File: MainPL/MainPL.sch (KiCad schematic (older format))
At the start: 37 parts, among them J1 Conn_01x06_Female, J10 Conn_01x06_Female, J11 Conn_01x06_Female, J12 Conn_01x06_Female, J13 Conn_01x06_Female, J14 Conn_01x06_Female, J15 Conn_01x01_Male, J16 Conn_01x04_Male, J2 USB_B, J3 Conn_01x06_Female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

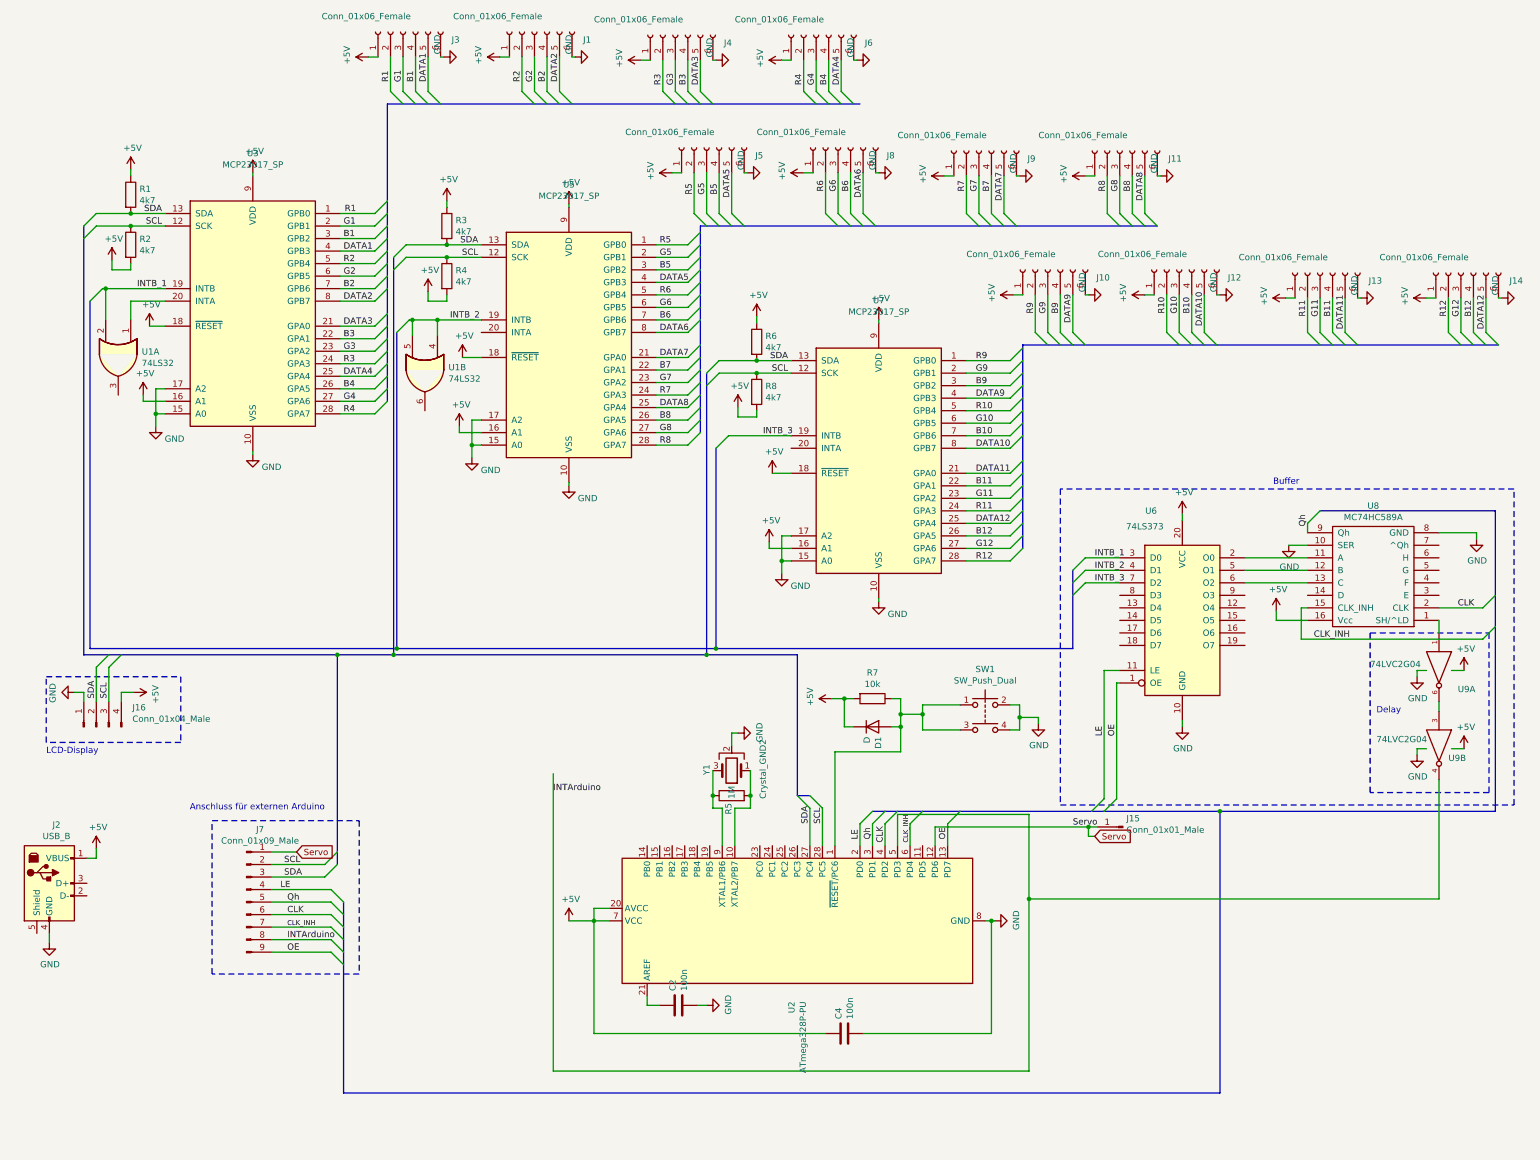
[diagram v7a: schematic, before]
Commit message: Änderung der Ints und leichte Verbesserung
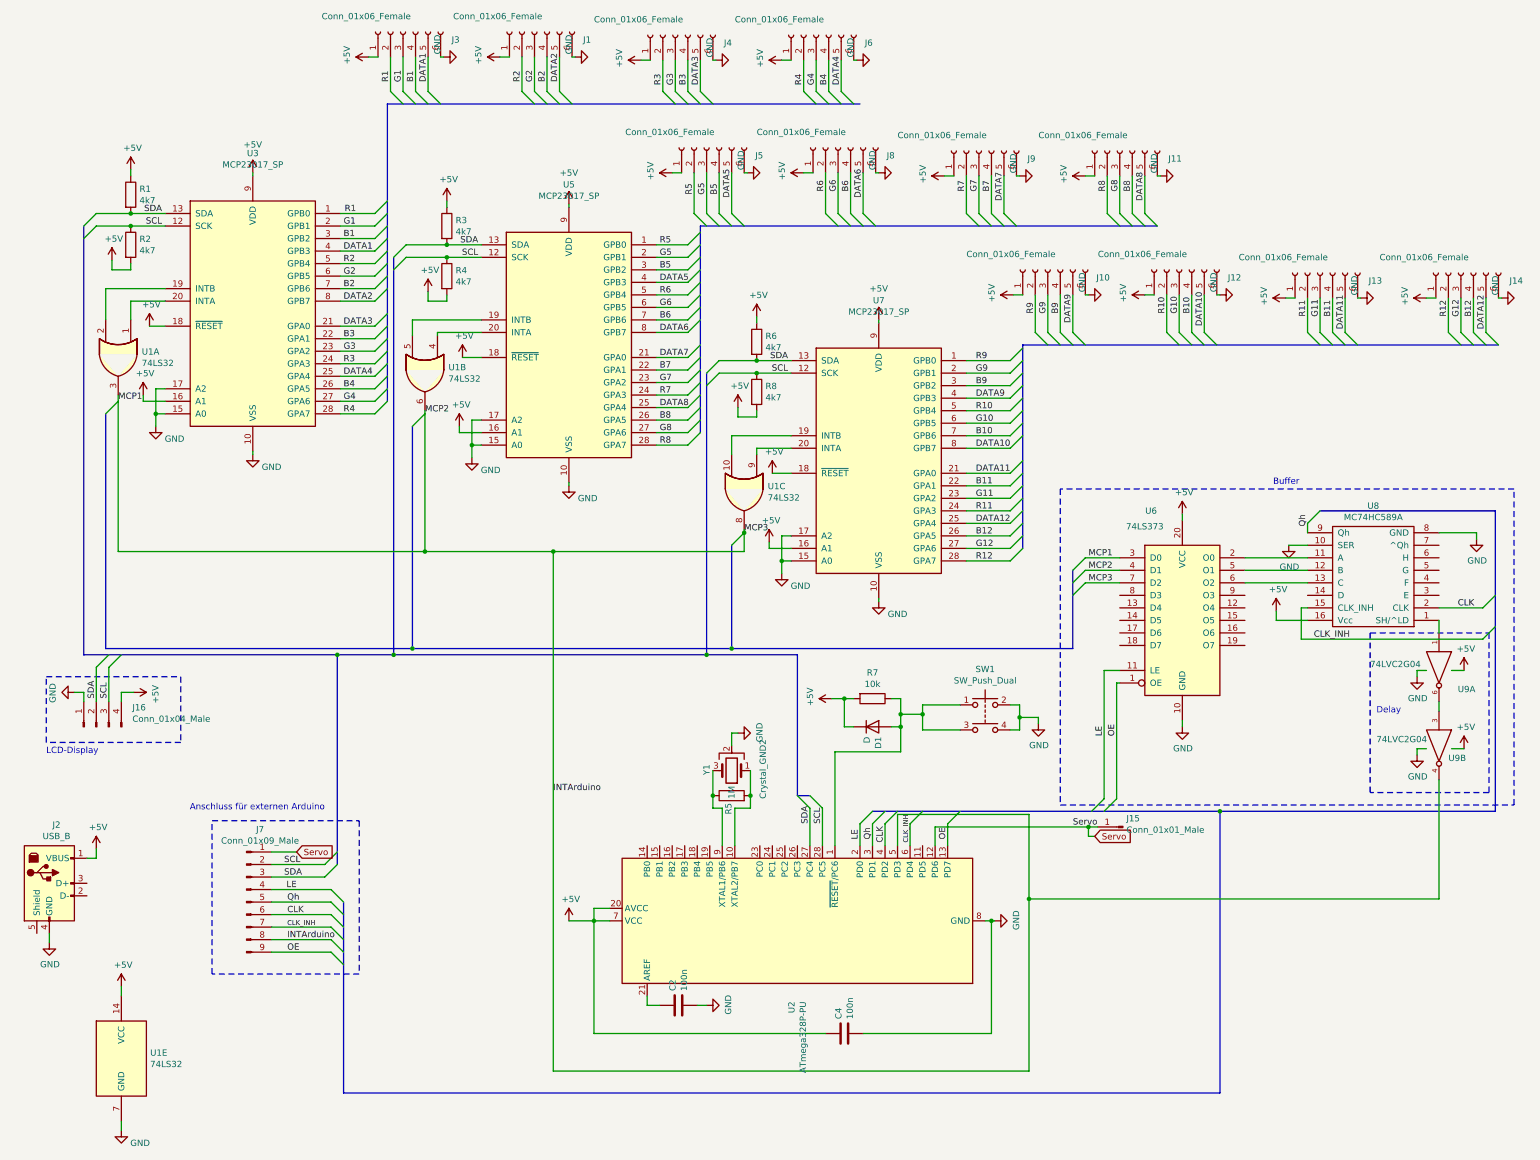
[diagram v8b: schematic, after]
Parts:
- added unit 3 of U1
- added unit 5 of U1
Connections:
- net +5V: now also U1.14 (VCC)
- net GND: now also U1.7 (GND)
- net INTArduino: now also U1.3, U1.6, U6.3 (D0), U6.4 (D1), U6.7 (D2), U1.8
- net at U5.20 (INTA): now also U1.4
- net at U7.20 (INTA): now also U1.9
- net INTB_1: no longer names the net of U1.2, U3.19 (INTB)
- net INTB_1: no longer U6.3 (D0)
- net INTB_2: no longer names the net of U1.5, U5.19 (INTB)
- net INTB_2: no longer U1.4, U6.4 (D1)
- net INTB_3: no longer names the net of U7.19 (INTB)
- net INTB_3: now also U1.10; no longer U6.7 (D2)
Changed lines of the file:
@@
 P 2600 1800
 F 0 "#PWR03" H 2600 1650 50  0001 C CNN
-F 1 "+5V" H 2615 1973 50  0000 C CNN
+F 1 "+5V" H 2600 2025 50  0000 C CNN
 F 2 "" H 2600 1800 50  0001 C CNN
 F 3 "" H 2600 1800 50  0001 C CNN
@@
 P 5125 2050
 F 0 "#PWR019" H 5125 1900 50  0001 C CNN
-F 1 "+5V" H 5140 2223 50  0000 C CNN
+F 1 "+5V" H 5125 2300 50  0000 C CNN
 F 2 "" H 5125 2050 50  0001 C CNN
 F 3 "" H 5125 2050 50  0001 C CNN
@@
 P 7600 2975
 F 0 "#PWR038" H 7600 2825 50  0001 C CNN
-F 1 "+5V" H 7615 3148 50  0000 C CNN
+F 1 "+5V" H 7600 3225 50  0000 C CNN
 F 2 "" H 7600 2975 50  0001 C CNN
 F 3 "" H 7600 2975 50  0001 C CNN
@@
 	10025 6175 10025 6225
 Entry Wire Line
-	1300 2825 1400 2725
-Entry Wire Line
-	3750 3075 3850 2975
-Entry Wire Line
-	6400 3900 6300 4000
-Wire Bus Line
-	1300 5600 3750 5600
-Connection ~ 3750 5600
-Wire Bus Line
-	3750 5600 6300 5600
-Connection ~ 6300 5600
-Wire Bus Line
-	6300 5600 9150 5600
-Entry Wire Line
 	9150 4975 9250 4875
 Entry Wire Line
@@
 Wire Wire Line
 	9525 5075 9250 5075
-Text Label 1675 2725 0    50   ~ 0
-INTB_1
-Text Label 4175 2975 0    50   ~ 0
-INTB_2
-Text Label 6675 3900 0    50   ~ 0
-INTB_3
 $Comp
 L Switch:SW_Push_Dual SW1
@@
 	0    1    1    0
 $EndComp
-Wire Bus Line
-	1300 2825 1300 5600
-Wire Bus Line
-	3750 3075 3750 5600
-Wire Bus Line
-	6300 4000 6300 5600
-Text Label 9325 4875 0    50   ~ 0
-INTB_1
-Text Label 9325 4975 0    50   ~ 0
-INTB_2
-Text Label 9325 5075 0    50   ~ 0
-INTB_3
 $Comp
 L power:GND #PWR055
@@
 Text Label 8150 7125 1    50   ~ 0
 OE
-Wire Wire Line
-	5000 6600 5000 8975
 Wire Wire Line
 	8050 7025 9275 7025
@@
 Wire Notes Line
 	11525 6750 11525 5475
-Text Label 2900 7525 2    50   ~ 0
+Text Label 2950 7525 2    50   ~ 0
 LE
 Text Label 2875 7625 0    50   ~ 0
@@
 LCD-Display
 Wire Wire Line
-	1400 2725 1425 2725
-Wire Wire Line
 	1425 2975 1425 2725
-Connection ~ 1425 2725
 Wire Wire Line
 	1425 2725 1900 2725
@@
 	1625 2825 1900 2825
 Wire Wire Line
-	3850 2975 3875 2975
-Wire Wire Line
 	3875 3100 3875 2975
-Connection ~ 3875 2975
-Wire Wire Line
-	3875 2975 4075 2975
-Wire Wire Line
-	4075 3100 4075 2975
+Wire Wire Line
+	3875 2975 4425 2975
+Wire Wire Line
+	4075 3100 4075 3075
+Wire Wire Line
+	4075 3075 4425 3075
+$Comp
+L 74xx:74LS32 U1
+U 3 1 5E1E7FA0
+P 6525 4350
+F 0 "U1" V 6479 4538 50  0000 L CNN
+F 1 "74LS32" V 6570 4538 50  0000 L CNN
+F 2 "" H 6525 4350 50  0001 C CNN
+F 3 "http://www.ti.com/lit/gpn/sn74LS32" H 6525 4350 50  0001 C CNN
+	3    6525 4350
+	0    1    1    0
+$EndComp
+Wire Wire Line
+	6425 4050 6425 3900
+Wire Wire Line
+	6425 3900 6900 3900
+Wire Wire Line
+	6625 4050 6625 4000
+Wire Wire Line
+	6625 4000 6900 4000
+Wire Bus Line
+	9150 5600 6425 5600
+Wire Bus Line
+	3875 5600 3875 3825
+Connection ~ 3875 5600
+Wire Bus Line
+	6425 5600 6425 4775
+Connection ~ 6425 5600
+Wire Bus Line
+	6425 5600 3875 5600
+Entry Wire Line
+	6425 4775 6525 4675
+Entry Wire Line
+	3875 3825 3975 3725
+Entry Wire Line
+	1425 3725 1525 3625
+Wire Bus Line
+	1425 3725 1425 5600
+Wire Bus Line
+	1425 5600 3875 5600
+Text Label 6525 4675 0    50   ~ 0
+MCP3
+Text Label 3975 3725 0    50   ~ 0
+MCP2
+Text Label 1525 3625 0    50   ~ 0
+MCP1
+Text Label 9275 5075 0    50   ~ 0
+MCP3
+Text Label 9275 4975 0    50   ~ 0
+MCP2
+Text Label 9275 4875 0    50   ~ 0
+MCP1
+$Comp
+L 74xx:74LS32 U1
+U 5 1 5E321082
+P 1550 8875
+F 0 "U1" H 1780 8921 50  0000 L CNN
+F 1 "74LS32" H 1780 8830 50  0000 L CNN
+F 2 "" H 1550 8875 50  0001 C CNN
+F 3 "http://www.ti.com/lit/gpn/sn74LS32" H 1550 8875 50  0001 C CNN
+	5    1550 8875
+	1    0    0    -1
+$EndComp
+$Comp
+L power:GND #PWR0105
+U 1 1 5E32718B
+P 1550 9450
+F 0 "#PWR0105" H 1550 9200 50  0001 C CNN
+F 1 "GND" H 1700 9350 50  0000 C CNN
+F 2 "" H 1550 9450 50  0001 C CNN
+F 3 "" H 1550 9450 50  0001 C CNN
+	1    1550 9450
+	1    0    0    -1
+$EndComp
+$Comp
+L power:+5V #PWR0106
+U 1 1 5E327769
+P 1550 8300
+F 0 "#PWR0106" H 1550 8150 50  0001 C CNN
+F 1 "+5V" H 1565 8473 50  0000 C CNN
+F 2 "" H 1550 8300 50  0001 C CNN
+F 3 "" H 1550 8300 50  0001 C CNN
+	1    1550 8300
+	1    0    0    -1
+$EndComp
+Wire Wire Line
+	1550 8300 1550 8375
+Wire Wire Line
+	1550 9450 1550 9375
+Wire Wire Line
+	5000 4825 3975 4825
+Wire Wire Line
+	5000 4825 5000 8975
+Connection ~ 3975 4825
+Wire Wire Line
+	3975 4825 1525 4825
+Wire Wire Line
+	5000 4825 6525 4825
+Wire Wire Line
+	6525 4650 6525 4675
+Wire Wire Line
+	3975 3700 3975 4825
+Wire Wire Line
+	1525 3575 1525 4825
+Wire Bus Line
+	3275 5650 3275 7325
 Wire Bus Line
 	1250 2225 1250 5650
@@
 	3725 2475 3725 5650
 Wire Bus Line
-	3275 5650 3275 7325
-Wire Bus Line
 	1250 5650 3275 5650
 Wire Bus Line
@@
 Wire Bus Line
 	3675 1250 7450 1250
-Connection ~ 4075 2975
-Wire Wire Line
-	4075 2975 4425 2975
-Wire Wire Line
-	6400 3900 6900 3900
+Connection ~ 5000 4825
+Connection ~ 6525 4675
+Wire Wire Line
+	6525 4675 6525 4825
 $EndSCHEMATC
